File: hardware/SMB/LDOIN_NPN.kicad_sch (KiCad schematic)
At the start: 5 parts, among them Q1 ZXTN4004KTC

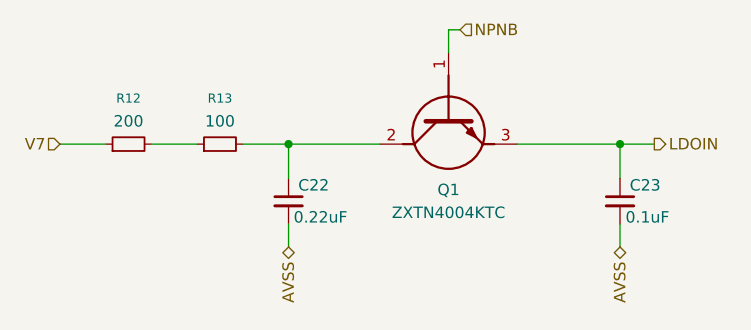
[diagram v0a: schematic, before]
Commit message: added BOM
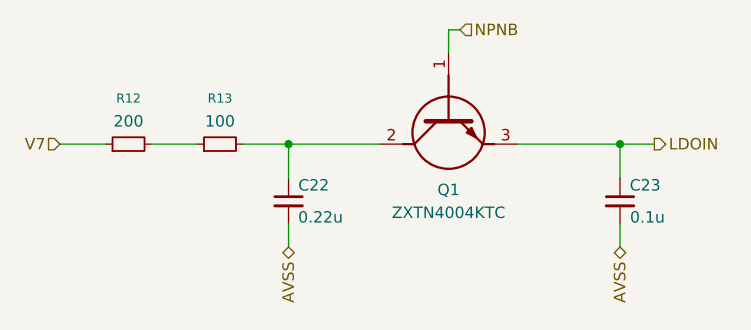
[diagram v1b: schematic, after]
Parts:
- C22: value 0.22uF -> 0.22u; P/N (none) -> CC0603KRX7R9BB224
- C23: value 0.1uF -> 0.1u; P/N (none) -> CL10B104KB8NNNC
- Q1: Height 2.52 -> (none); Manufacturer_Name Diodes Incorporated -> (none); Manufacturer_Part_Number ZXTN4004KTC -> (none); Mouser Part Number 621-ZXTN4004KTC -> (none); Mouser Price/Stock https://www.mouser.co.uk/ProductDetail/Diodes-Incorporated/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 -> (none); P/N (none) -> ZXTN4004KTC
- R12: P/N (none) -> RC0603FR-07200RL
- R13: P/N (none) -> 0603WAF1000T5E
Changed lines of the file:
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@@
+			)
+		)
+		(property "P/N" "RC0603FR-07200RL"
+			(at 109.22 105.41 90)
+			(hide yes)
+			(show_name no)
+			(do_not_autoplace no)
+			(effects
+				(font
+					(size 1.27 1.27)
+				)
 			)
 		)
@@
 			)
 		)
-		(property "Height" "2.52"
-			(at 546.05 109.22 0)
-			(hide yes)
-			(show_name no)
-			(do_not_autoplace no)
-			(effects
-				(font
-					(size 1.27 1.27)
-				)
-				(justify left top)
-			)
-		)
-		(property "Mouser Part Number" "621-ZXTN4004KTC"
-			(at 646.05 109.22 0)
-			(hide yes)
-			(show_name no)
-			(do_not_autoplace no)
-			(effects
-				(font
-					(size 1.27 1.27)
-				)
-				(justify left top)
-			)
-		)
-		(property "Mouser Price/Stock" "https://www.mouser.co.uk/ProductDetail/Diodes-Incorporated/ZXTN4004KTC?qs=aXnpsjvrXd1NjskJTVsVYA%3D%3D"
-			(at 746.05 109.22 0)
-			(hide yes)
-			(show_name no)
-			(do_not_autoplace no)
-			(effects
-				(font
-					(size 1.27 1.27)
-				)
-				(justify left top)
-			)
-		)
-		(property "Manufacturer_Name" "Diodes Incorporated"
-			(at 846.05 109.22 0)
-			(hide yes)
-			(show_name no)
-			(do_not_autoplace no)
-			(effects
-				(font
-					(size 1.27 1.27)
-				)
-				(justify left top)
-			)
-		)
-		(property "Manufacturer_Part_Number" "ZXTN4004KTC"
-			(at 946.05 109.22 0)
-			(hide yes)
-			(show_name no)
-			(do_not_autoplace no)
-			(effects
-				(font
-					(size 1.27 1.27)
-				)
-				(justify left top)
+		(property "P/N" "ZXTN4004KTC"
+			(at 144.78 95.25 90)
+			(hide yes)
+			(show_name no)
+			(do_not_autoplace no)
+			(effects
+				(font
+					(size 1.27 1.27)
+				)
 			)
 		)
@@
 			)
 		)
-		(property "Value" "0.22uF"
+		(property "Value" "0.22u"
 			(at 130.556 113.538 0)
 			(show_name no)
@@
 		)
 		(property "Description" "Unpolarized capacitor, small symbol"
+			(at 127 111.76 0)
+			(hide yes)
+			(show_name no)
+			(do_not_autoplace no)
+			(effects
+				(font
+					(size 1.27 1.27)
+				)
+			)
+		)
+		(property "P/N" "CC0603KRX7R9BB224"
 			(at 127 111.76 0)
 			(hide yes)
@@
 			)
 		)
+		(property "P/N" "0603WAF1000T5E"
+			(at 119.38 105.41 90)
+			(hide yes)
+			(show_name no)
+			(do_not_autoplace no)
+			(effects
+				(font
+					(size 1.27 1.27)
+				)
+			)
+		)
 		(pin "1"
 		)
@@
 			)
 		)
-		(property "Value" "0.1uF"
+		(property "Value" "0.1u"
 			(at 166.878 113.538 0)
 			(show_name no)
@@
 			(at 163.83 111.76 0)
 			(hide yes)
+			(show_name no)
+			(do_not_autoplace no)
+			(effects
+				(font
+					(size 1.27 1.27)
+				)
+			)
+		)
+		(property "P/N" "CL10B104KB8NNNC"
+			(at 163.83 111.76 0)
+			(hide yes)
